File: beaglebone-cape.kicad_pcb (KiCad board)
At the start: 2 copper layers, 86.4 x 54.6 mm, 56 parts, among them P1 BEAGLEBONE_BLACK, P4 JUMPERS, Q1 2N7000, Q2 2N7000, Q3 2N7000, Q4 2N7000, U2 V7805-2000, U3 4N25, U4 4N25

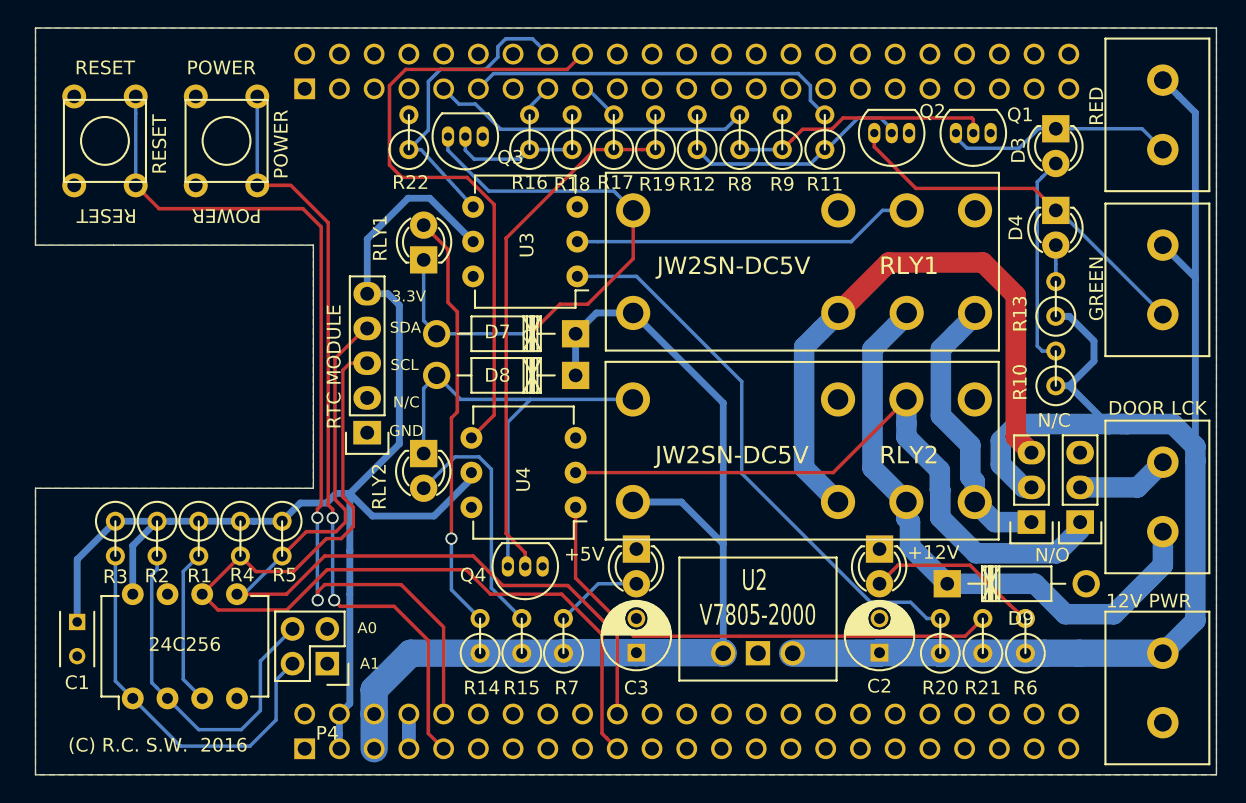
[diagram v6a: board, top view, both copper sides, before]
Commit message: tweaking silk screen, checked dimensions, ready for mfg
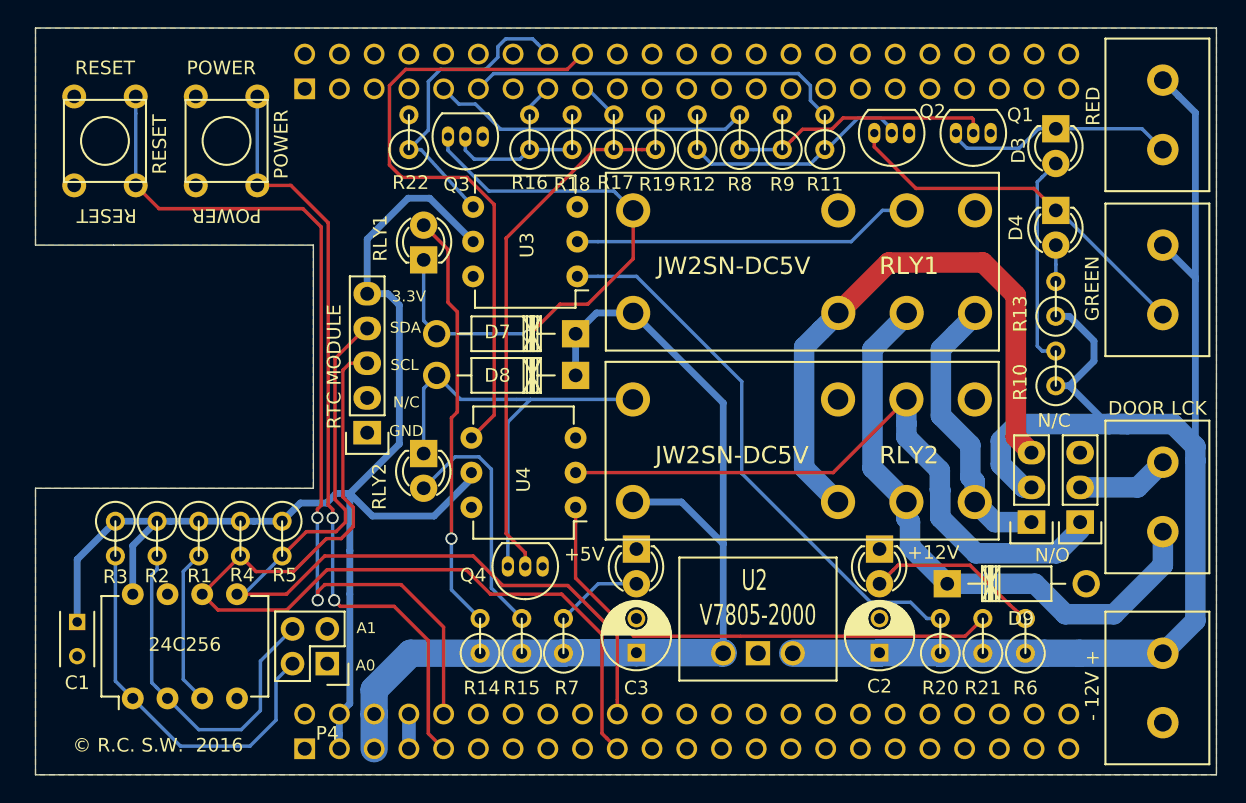
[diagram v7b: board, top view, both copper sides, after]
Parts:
- - 12V +: renamed from 12V PWR
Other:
- board text added: "+ -"
- board text added: "12V"
- board text added: "DOOR LOCK"
- board text added: "GREEN LIGHT"
- board text added: "RED LIGHT"
- board text added: "© R.C. S.W. 2016"
- board text added: "© R.C., S.W. 2016"
- board text removed: "(C) R.C. S.W. 2016"
- board text removed: "(C) R.C., S.W. 2016"
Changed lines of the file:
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@@
     (area 93.8824 84.786399 182.7236 140.1786)
     (thickness 1.6)
-    (drawings 25)
+    (drawings 33)
     (tracks 375)
     (zones 0)
@@
   (title_block
     (title "BeagleBone Black Cape")
-    (date 2016-01-10)
-    (rev 1.3)
+    (date 2016-01-11)
+    (rev 1.31)
     (comment 1 "License: GPL v3, https://github.com/bubbapizza/BBBdc")
     (comment 2 "Design by Rob Caruso")
@@
     (visible_elements 7FFFF7FF)
     (pcbplotparams
-      (layerselection 0x00030_80000001)
+      (layerselection 0x010f0_80000001)
       (usegerberextensions true)
       (excludeedgelayer true)
@@
       (drillshape 0)
       (scaleselection 1)
-      (outputdirectory ""))
+      (outputdirectory mfg/))
   )
   (net 0 "")
@@
     (descr "TO-92 leads in-line, narrow, oval pads, drill 0.6mm (see NXP sot054_po.pdf)")
     (tags "to-92 sc-43 sc-43a sot54 PA33 transistor")
-    (fp_text reference Q3 (at -2.032 -1.525 180) (layer F.SilkS)
+    (fp_text reference Q3 (at 1.905 -3.4925 180) (layer F.SilkS)
       (effects (font (size 1 1) (thickness 0.15)))
     )
@@
     (at 176.53 133.35 90)
     (descr "2-way 2.54mm pitch terminal block, Phoenix MPT series")
-    (fp_text reference "12V PWR" (at 6.35 -0.635 180) (layer F.SilkS)
+    (fp_text reference "- 12V +" (at 0.1905 -4.7625 90) (layer F.SilkS)
       (effects (font (size 1 1) (thickness 0.15)))
     )
@@
     (at 176.53 91.44 90)
     (descr "2-way 2.54mm pitch terminal block, Phoenix MPT series")
-    (fp_text reference RED (at 0.635 -4.445 90) (layer F.SilkS)
+    (fp_text reference RED (at 0.635 -4.699 90) (layer F.SilkS)
       (effects (font (size 1 1) (thickness 0.15)))
     )
@@
     (at 176.53 103.505 90)
     (descr "2-way 2.54mm pitch terminal block, Phoenix MPT series")
-    (fp_text reference GREEN (at -0.635 -4.445 90) (layer F.SilkS)
+    (fp_text reference GREEN (at -0.635 -4.7625 90) (layer F.SilkS)
       (effects (font (size 1 1) (thickness 0.15)))
     )
@@
     )
   )
-  (gr_text "(C) R.C., S.W.  2016" (at 103.5685 137.6045) (layer B.SilkS)
+  (gr_text "GREEN LIGHT" (at 174.371 103.3145 90) (layer B.SilkS)
     (effects (font (size 1 1) (thickness 0.15)) (justify mirror))
   )
-  (gr_text "(C) R.C. S.W.  2016" (at 103.4415 137.541) (layer F.SilkS)
+  (gr_text "RED LIGHT" (at 174.244 91.5035 90) (layer B.SilkS)
+    (effects (font (size 1 1) (thickness 0.15)) (justify mirror))
+  )
+  (gr_text "+      -" (at 179.2605 91.694 90) (layer B.SilkS)
+    (effects (font (size 1 1) (thickness 0.15)) (justify mirror))
+  )
+  (gr_text "+      -" (at 179.2605 103.759 90) (layer B.SilkS)
+    (effects (font (size 1 1) (thickness 0.15)) (justify mirror))
+  )
+  (gr_text "+      -" (at 179.3875 133.477 90) (layer B.SilkS)
+    (effects (font (size 1 1) (thickness 0.15)) (justify mirror))
+  )
+  (gr_text 12V (at 174.3075 133.4135 90) (layer B.SilkS)
+    (effects (font (size 1 1) (thickness 0.15)) (justify mirror))
+  )
+  (gr_text "+      -" (at 179.451 119.38 270) (layer B.SilkS)
+    (effects (font (size 1 1) (thickness 0.15)) (justify mirror))
+  )
+  (gr_text "DOOR LOCK" (at 174.244 119.4435 90) (layer B.SilkS)
+    (effects (font (size 1 1) (thickness 0.15)) (justify mirror))
+  )
+  (gr_text "© R.C., S.W.  2016" (at 103.5685 137.6045) (layer B.SilkS)
+    (effects (font (size 1 1) (thickness 0.15)) (justify mirror))
+  )
+  (gr_text "© R.C. S.W.  2016" (at 103.4415 137.541) (layer F.SilkS)
     (effects (font (size 1 1) (thickness 0.15)))
   )
@@
     (effects (font (size 1 1) (thickness 0.15)))
   )
-  (gr_text A0 (at 118.745 128.9685) (layer F.SilkS)
+  (gr_text A0 (at 118.618 131.699) (layer F.SilkS)
     (effects (font (size 0.8 0.8) (thickness 0.15)))
   )
-  (gr_text A1 (at 118.9355 131.572) (layer F.SilkS)
+  (gr_text A1 (at 118.6815 128.9685) (layer F.SilkS)
     (effects (font (size 0.8 0.8) (thickness 0.15)))
   )

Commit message: renamed hocuspocus library to abracadabra, fixed mask on panasonic relay library module, added R23, fixed wiring for relays
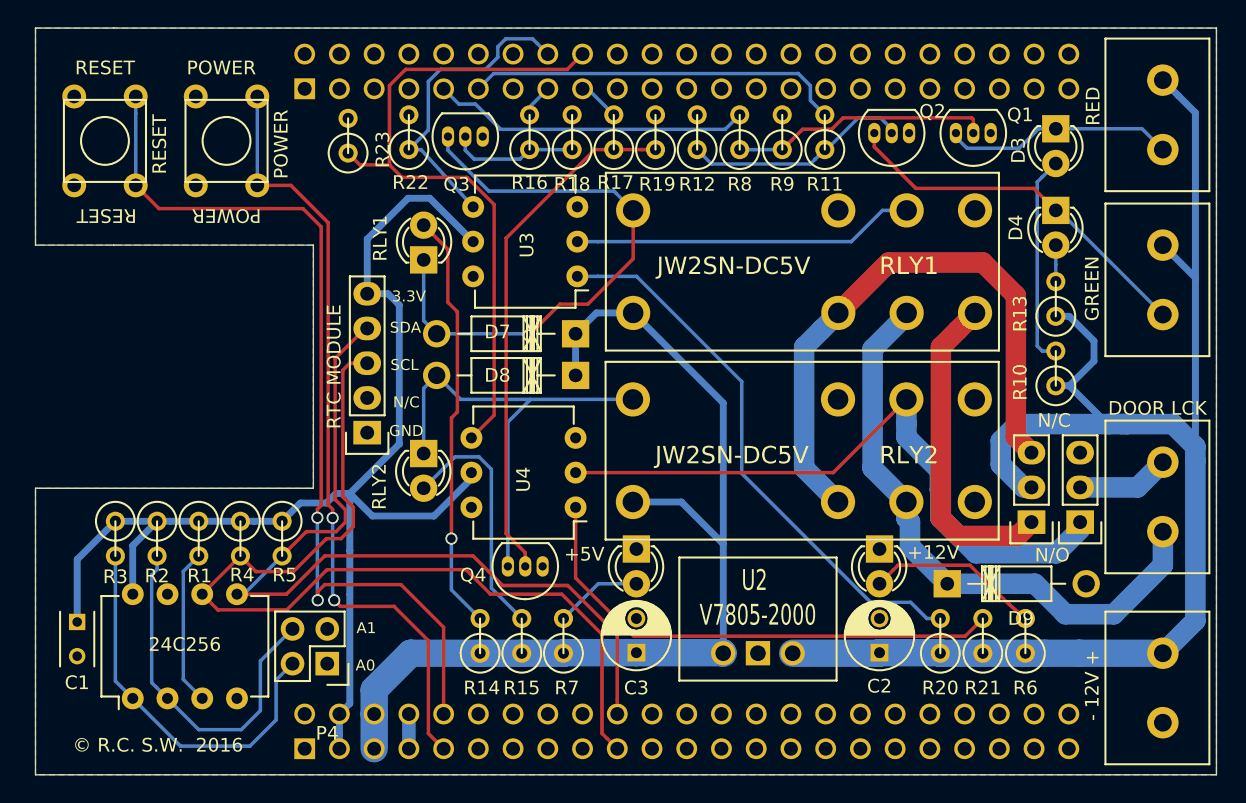
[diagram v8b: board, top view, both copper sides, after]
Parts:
- added R23: 2k, Discret:R1, F.Cu at (117.3, 93.0)
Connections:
- RLY2 pad 4: Net-(P8-Pad1) -> Net-(RLY2-Pad4)
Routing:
- net /LOCK_RELAYS/R2_READ: track 47.5 -> 50.9 mm
- net Net-(P8-Pad1): track 20.3 -> 23.6 mm
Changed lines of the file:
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@@
-(kicad_pcb (version 4) (host pcbnew 4.0.1-3.201512221401+6198~38~ubuntu15.10.1-stable)
+(kicad_pcb (version 4) (host pcbnew 4.0.2+e4-6225~38~ubuntu15.10.1-stable)
   (general
-    (links 126)
-    (no_connects 0)
-    (area 93.8824 84.786399 182.7236 140.1786)
+    (links 127)
+    (no_connects 2)
+    (area 94.437999 85.039999 180.898001 139.750001)
     (thickness 1.6)
     (drawings 33)
-    (tracks 375)
+    (tracks 374)
     (zones 0)
-    (modules 56)
-    (nets 115)
+    (modules 57)
+    (nets 116)
   )
   (page A)
@@
   (net 113 "Net-(U3-Pad6)")
   (net 114 "Net-(U4-Pad6)")
+  (net 115 "Net-(RLY2-Pad4)")
   (net_class Default "This is the default net class."
     (clearance 0.2286)
@@
     (add_net "Net-(RLY1-Pad6)")
     (add_net "Net-(RLY1-Pad7)")
+    (add_net "Net-(RLY2-Pad4)")
     (add_net "Net-(RLY2-Pad7)")
     (add_net "Net-(U1-Pad7)")
@@
       (net 21 "Net-(D9-Pad1)"))
     (pad 4 thru_hole circle (at 10.5 3.75) (size 2.5 2.5) (drill 1.5) (layers *.Cu F.Paste F.SilkS F.Mask)
-      (net 101 "Net-(P8-Pad1)"))
+      (net 115 "Net-(RLY2-Pad4)"))
     (pad 5 thru_hole circle (at 10.5 -3.75) (size 2.5 2.5) (drill 1.5) (layers *.Cu F.Paste F.SilkS F.Mask)
       (net 7 GND))
@@
       (scale (xyz 1 1 1))
       (rotate (xyz 0 0 90))
+    )
+  )
+  (module Discret:R1 (layer F.Cu)
+    (at 117.348 92.964 90)
+    (descr "Resistance verticale")
+    (tags R)
+    (fp_text reference R23 (at -1.016 2.54 90) (layer F.SilkS)
+      (effects (font (size 1 1) (thickness 0.15)))
+    )
+    (fp_text value 2k (at -1.143 2.54 90) (layer F.Fab)
+      (effects (font (size 1 1) (thickness 0.15)))
+    )
+    (fp_line (start -1.27 0) (end 1.27 0) (layer F.SilkS) (width 0.15))
+    (fp_circle (center -1.27 0) (end -0.635 1.27) (layer F.SilkS) (width 0.15))
+    (pad 1 thru_hole circle (at -1.27 0 90) (size 1.397 1.397) (drill 0.8128) (layers *.Cu *.Mask F.SilkS)
+      (net 37 /LOCK_RELAYS/R2_READ))
+    (pad 2 thru_hole circle (at 1.27 0 90) (size 1.397 1.397) (drill 0.8128) (layers *.Cu *.Mask F.SilkS)
+      (net 7 GND))
+    (model Discret.3dshapes/R1.wrl
+      (at (xyz 0 0 0))
+      (scale (xyz 1 1 1))
+      (rotate (xyz 0 0 0))
     )
   )
@@
   (segment (start 136.779 91.44) (end 134.874 89.535) (width 0.254) (layer B.Cu) (net 36))
   (segment (start 134.874 89.535) (end 134.493 89.535) (width 0.254) (layer B.Cu) (net 36))
+  (segment (start 120.370601 95.097601) (end 118.211601 95.097601) (width 0.254) (layer F.Cu) (net 37))
+  (segment (start 118.211601 95.097601) (end 117.348 94.234) (width 0.254) (layer F.Cu) (net 37))
   (segment (start 134.493 86.995) (end 133.375399 88.112601) (width 0.254) (layer F.Cu) (net 37))
   (segment (start 133.375399 88.112601) (end 121.561349 88.112601) (width 0.254) (layer F.Cu) (net 37))
@@
   (segment (start 170.8785 118.6815) (end 175.0885 118.6815) (width 1.5) (layer B.Cu) (net 100))
   (segment (start 175.0885 118.6815) (end 176.93 116.84) (width 1.5) (layer B.Cu) (net 100))
-  (segment (start 161.777001 107.488999) (end 163.027 106.239) (width 1.5) (layer B.Cu) (net 101))
-  (segment (start 163.176 119.75) (end 163.176 118.257962) (width 1.5) (layer B.Cu) (net 101))
-  (segment (start 163.176 118.257962) (end 162.849279 117.931241) (width 1.5) (layer B.Cu) (net 101))
-  (segment (start 162.849279 117.931241) (end 162.849279 115.591608) (width 1.5) (layer B.Cu) (net 101))
-  (segment (start 162.849279 115.591608) (end 160.697399 113.439729) (width 1.5) (layer B.Cu) (net 101))
-  (segment (start 160.697399 113.439729) (end 160.697399 108.568601) (width 1.5) (layer B.Cu) (net 101))
-  (segment (start 160.697399 108.568601) (end 161.777001 107.488999) (width 1.5) (layer B.Cu) (net 101))
-  (segment (start 167.3225 121.2215) (end 164.6475 121.2215) (width 1.5) (layer B.Cu) (net 101))
-  (segment (start 164.6475 121.2215) (end 163.176 119.75) (width 1.5) (layer B.Cu) (net 101))
+  (segment (start 167.3225 121.2215) (end 166.315399 122.228601) (width 1.5) (layer F.Cu) (net 101))
+  (segment (start 166.315399 122.228601) (end 161.986271 122.228601) (width 1.5) (layer F.Cu) (net 101))
+  (segment (start 161.986271 122.228601) (end 160.697399 120.939729) (width 1.5) (layer F.Cu) (net 101))
+  (segment (start 160.697399 120.939729) (end 160.697399 108.422601) (width 1.5) (layer F.Cu) (net 101))
+  (segment (start 160.697399 108.422601) (end 161.945001 107.174999) (width 1.5) (layer F.Cu) (net 101))
+  (segment (start 161.945001 107.174999) (end 163.195 105.925) (width 1.5) (layer F.Cu) (net 101))
   (segment (start 167.3225 116.1415) (end 166.1795 114.9985) (width 1.5) (layer F.Cu) (net 102))
   (segment (start 156.885 102.235) (end 153.195 105.925) (width 1.5) (layer F.Cu) (net 102))
